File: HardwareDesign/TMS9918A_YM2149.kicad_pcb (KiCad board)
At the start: 2 copper layers, 150 x 90 mm, 46 parts, among them J001 Conn_02x40_Odd_Even, J701 RCJ-044, J702 Conn_01x02, J801 Conn_01x02, J802 Conn_02x09_Odd_Even, J803 SJ1-3525N, Q701 2N4401, U701 TMS9918A, U702 74HCT04, U703 74HCT32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

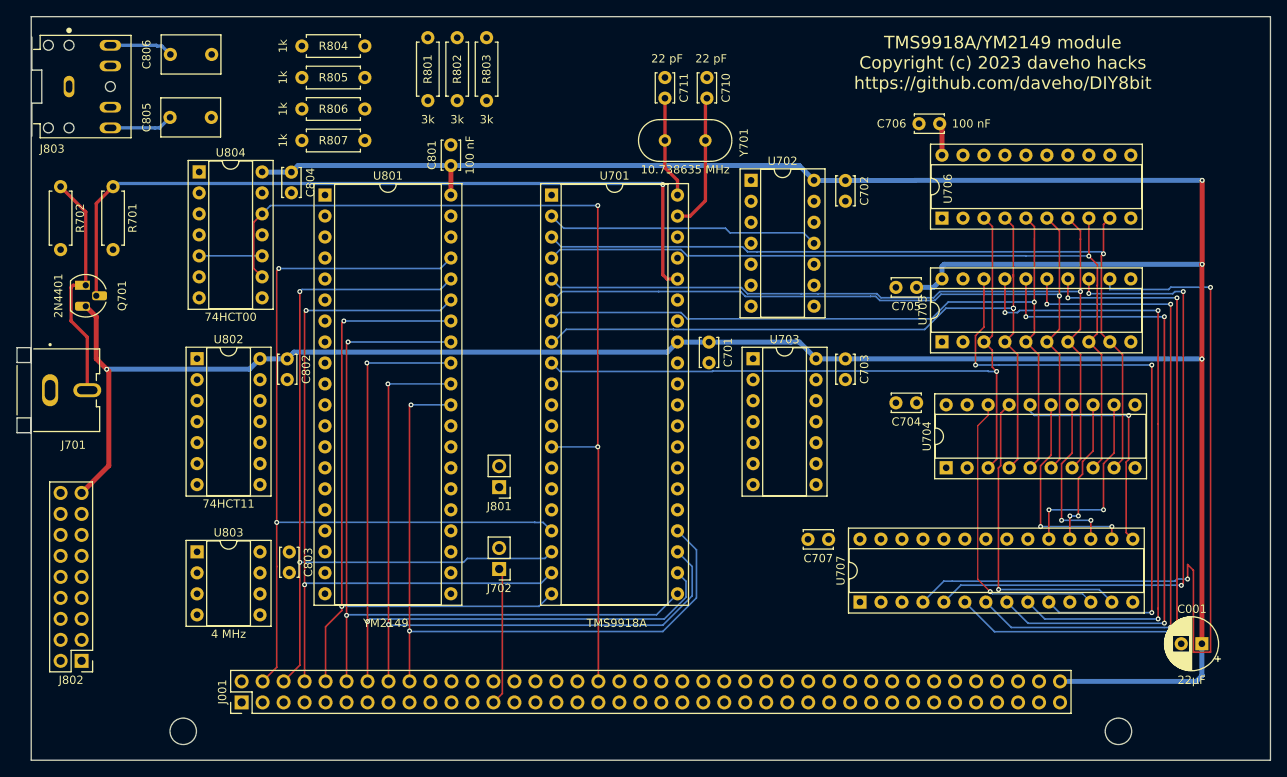
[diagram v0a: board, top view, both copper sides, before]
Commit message: completely started over on routing traces
Also, remove all Edge.Cuts lines from the 3.5mm audio jack
footprint. Not sure what those were supposed to be there
for, they definitely aren't needed.
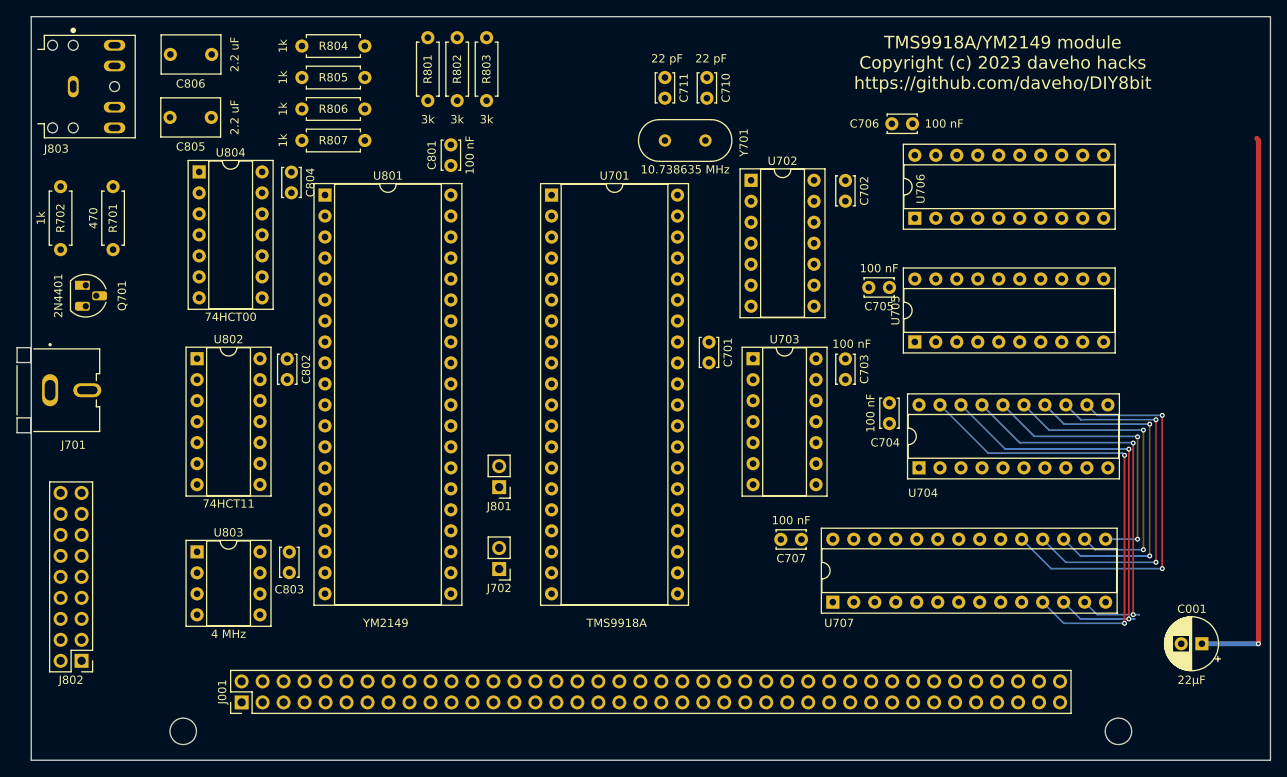
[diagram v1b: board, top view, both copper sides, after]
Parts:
- moved C704 3.29 mm to (167.4, 105.2), turned to -90 degrees
- moved C705 3.29 mm to (167.4, 91.2)
- moved C707 3.29 mm to (156.7, 121.7)
- moved U704 3.29 mm to (171.0, 113.0)
- moved U705 3.29 mm to (170.5, 97.8)
- moved U706 3.29 mm to (170.5, 82.8)
- moved U707 3.29 mm to (160.5, 129.3)
- moved C706 3.29 mm to (170.2, 71.4)
- moved J803 0.51 mm to (68.6, 66.9)
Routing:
- net VCC: track 396.4 -> 68.1 mm, vias 4 -> 1
- net /A0: track 113.0 -> 0.00 mm, vias 2 -> 0
- net /D0: track 105.8 -> 0.00 mm, vias 2 -> 0
- net /TMS9918ADisplay/VA6: track 105.7 -> 0.00 mm, vias 2 -> 0
- net /TMS9918ADisplay/AD7: track 99.8 -> 0.00 mm, vias 1 -> 0
- net /TMS9918ADisplay/AD6: track 98.2 -> 0.00 mm, vias 1 -> 0
- net /D1: track 97.9 -> 0.00 mm, vias 2 -> 0
- net /TMS9918ADisplay/AD5: track 97.8 -> 0.00 mm, vias 1 -> 0
- net /TMS9918ADisplay/AD4: track 95.3 -> 0.00 mm, vias 1 -> 0
- net /D4: track 94.7 -> 0.00 mm, vias 2 -> 0
- net Net-(Q701-Pad2): track 93.7 -> 0.00 mm, vias 1 -> 0
- net /D2: track 93.5 -> 0.00 mm, vias 2 -> 0
- net /TMS9918ADisplay/AD3: track 92.1 -> 0.00 mm, vias 1 -> 0
- net /D5: track 91.9 -> 0.00 mm, vias 2 -> 0
- net /TMS9918ADisplay/AD2: track 90.0 -> 0.00 mm, vias 2 -> 0
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
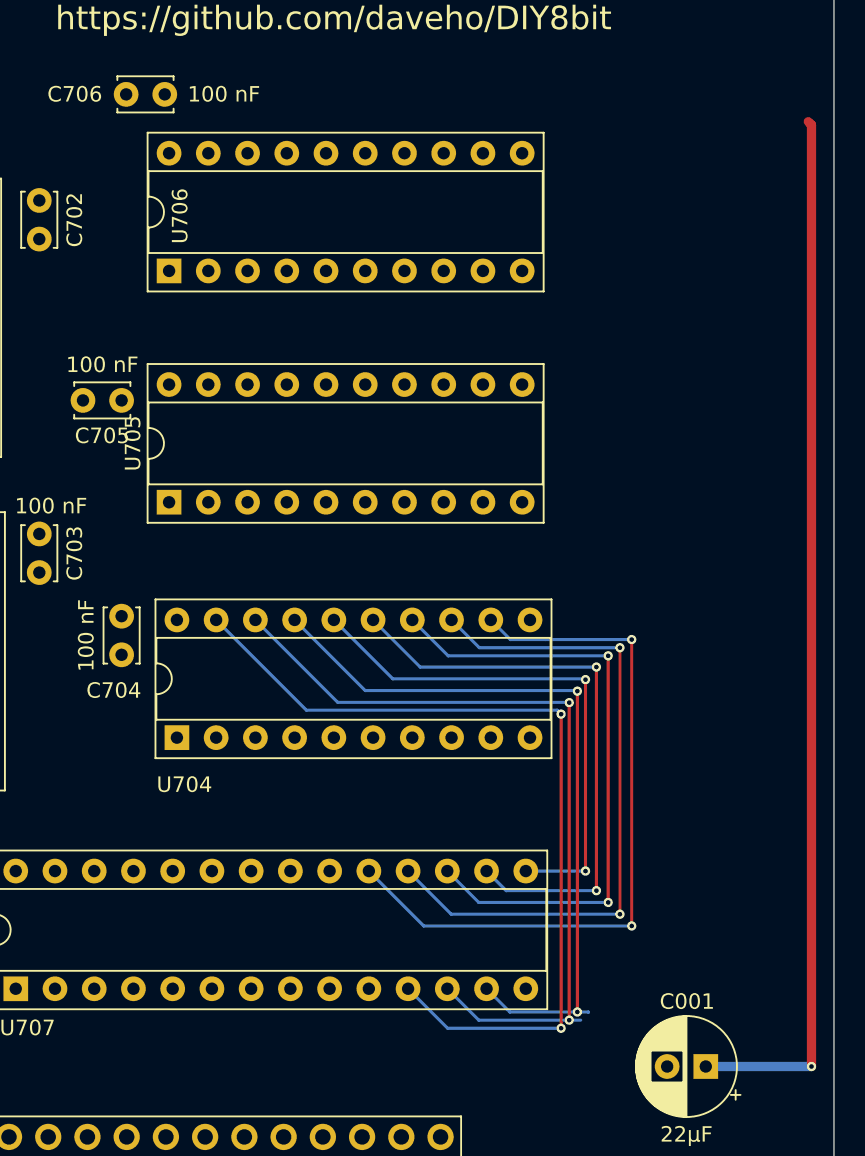
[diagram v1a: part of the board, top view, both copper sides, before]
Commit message: more routing of TMS9918A address/data reg signals
I think I have a viable strategy.
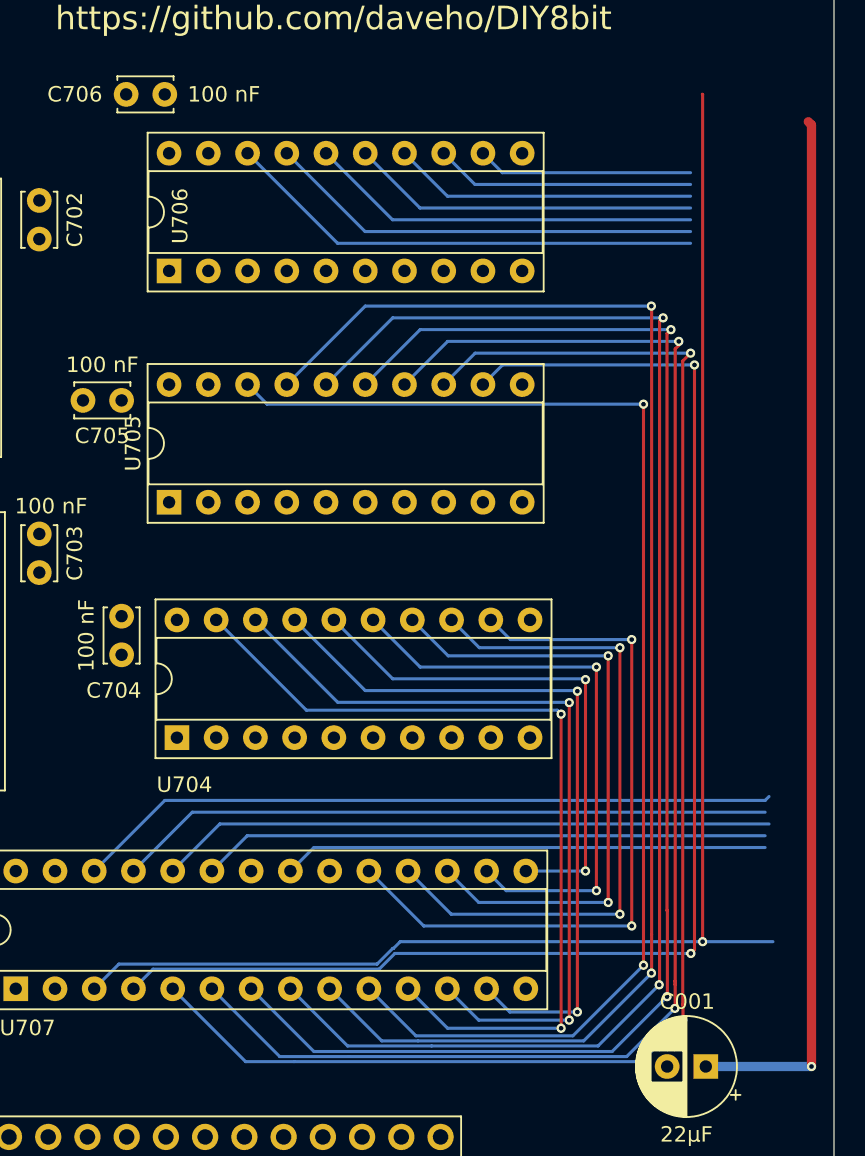
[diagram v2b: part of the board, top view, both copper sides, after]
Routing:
- net /TMS9918ADisplay/VA7: track 0.00 -> 131.2 mm, vias 0 -> 1
- net /TMS9918ADisplay/VA5: track 0.00 -> 96.3 mm, vias 0 -> 2
- net /TMS9918ADisplay/VA4: track 0.00 -> 95.5 mm, vias 0 -> 2
- net /TMS9918ADisplay/VA3: track 0.00 -> 94.6 mm, vias 0 -> 2
- net /TMS9918ADisplay/VA2: track 0.00 -> 94.2 mm, vias 0 -> 2
- net /TMS9918ADisplay/VA1: track 0.00 -> 93.0 mm, vias 0 -> 2
- net /TMS9918ADisplay/VA6: track 0.00 -> 89.4 mm, vias 0 -> 2
- net /TMS9918ADisplay/VA0: track 0.00 -> 83.4 mm, vias 0 -> 2
- net /TMS9918ADisplay/VA8: track 0.00 -> 70.7 mm
- net /TMS9918ADisplay/VA9: track 0.00 -> 65.3 mm
- net /TMS9918ADisplay/VA13: track 0.00 -> 59.7 mm
- net /TMS9918ADisplay/VA11: track 0.00 -> 56.4 mm
- net /TMS9918ADisplay/VA10: track 0.00 -> 53.9 mm
- net /TMS9918ADisplay/VA12: track 0.00 -> 16.8 mm
- net /TMS9918ADisplay/VD1: track 52.6 -> 51.8 mm
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
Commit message: routed more signals
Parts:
- moved J701 4.07 mm to (69.8, 103.9)
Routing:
- net VCC: track 68.1 -> 297.6 mm, vias 1 -> 5
- net /~{IODEV6}: track 0.00 -> 145.9 mm
- net /~{WMEM}: track 0.00 -> 145.2 mm, vias 0 -> 2
- net /~{RST}: track 0.00 -> 141.8 mm, vias 0 -> 3
- net /TMS9918ADisplay/VA12: track 16.8 -> 116.0 mm, vias 0 -> 2
- net /TMS9918ADisplay/V~{R}/W: track 0.00 -> 94.3 mm, vias 0 -> 3
- net /~{RMEM}: track 0.00 -> 63.9 mm, vias 0 -> 1
- net /TMS9918ADisplay/VR/~{W}: track 0.00 -> 63.6 mm, vias 0 -> 2
- net Net-(U702-Pad10): track 0.00 -> 51.6 mm, vias 0 -> 1
- net /TMS9918ADisplay/~{RAS}: track 0.00 -> 46.6 mm, vias 0 -> 1
- net /~{IODEV5}: track 0.00 -> 44.4 mm, vias 0 -> 1
- net /TMS9918ADisplay/VA13: track 59.7 -> 102.2 mm, vias 0 -> 2
- net /TMS9918ADisplay/VA11: track 56.4 -> 96.6 mm, vias 0 -> 2
- net /TMS9918ADisplay/VA10: track 53.9 -> 93.1 mm, vias 0 -> 2
- net /TMS9918ADisplay/VA9: track 65.3 -> 104.3 mm, vias 0 -> 2
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
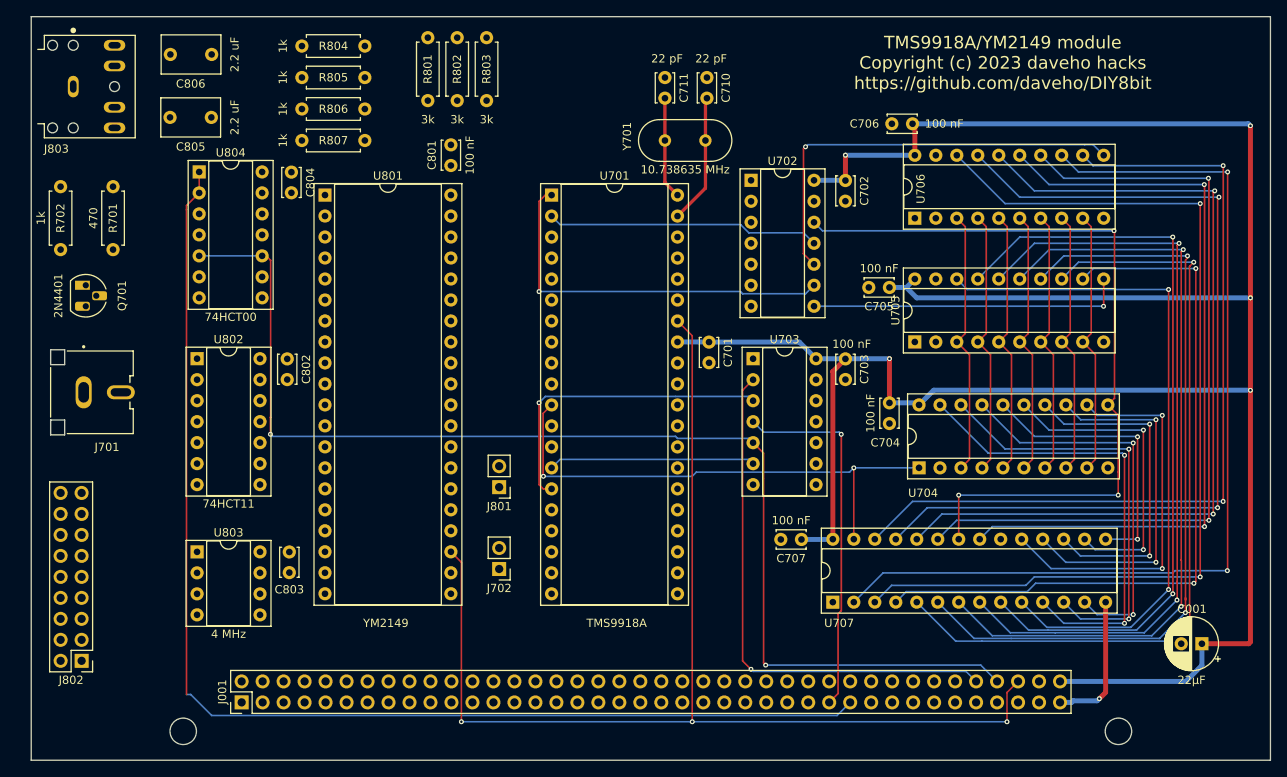
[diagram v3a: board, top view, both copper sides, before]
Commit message: TMS9918A section mostly done
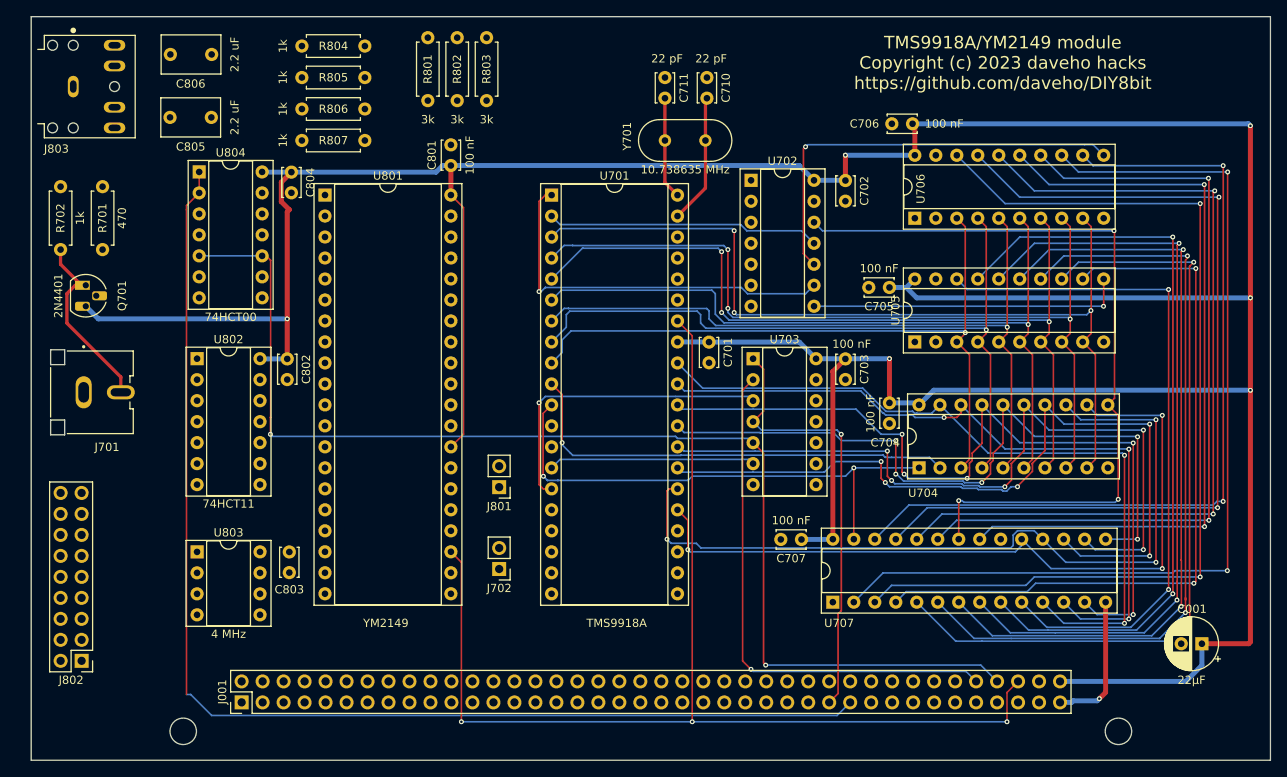
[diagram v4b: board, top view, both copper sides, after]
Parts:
- moved R701 7.73 mm to (72.1, 86.6), turned to 90 degrees
- moved R702 7.62 mm to (67.1, 86.6), turned to 90 degrees
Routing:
- net VCC: track 297.6 -> 452.7 mm, vias 5 -> 6
- net /TMS9918ADisplay/AD7: track 32.1 -> 108.2 mm, vias 0 -> 3
- net /TMS9918ADisplay/AD6: track 32.1 -> 103.8 mm, vias 0 -> 3
- net /TMS9918ADisplay/AD5: track 32.1 -> 102.2 mm, vias 0 -> 3
- net /TMS9918ADisplay/AD4: track 32.1 -> 93.6 mm, vias 0 -> 1
- net /TMS9918ADisplay/AD3: track 32.1 -> 89.7 mm, vias 0 -> 1
- net /TMS9918ADisplay/AD2: track 32.1 -> 88.7 mm, vias 0 -> 1
- net /TMS9918ADisplay/VD5: track 40.9 -> 97.0 mm, vias 2 -> 5
- net /TMS9918ADisplay/VD6: track 43.8 -> 98.9 mm, vias 2 -> 3
- net /TMS9918ADisplay/AD0: track 0.00 -> 54.8 mm, vias 0 -> 1
- net /TMS9918ADisplay/VD4: track 37.8 -> 92.2 mm, vias 2 -> 5
- net /TMS9918ADisplay/AD1: track 32.1 -> 84.9 mm, vias 0 -> 1
- net /TMS9918ADisplay/VD3: track 34.1 -> 86.7 mm, vias 2 -> 5
- net /TMS9918ADisplay/VD2: track 47.9 -> 98.9 mm, vias 2 -> 5
- net /TMS9918ADisplay/VD7: track 46.7 -> 93.6 mm, vias 2 -> 3
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
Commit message: routed more traces (getting there...)
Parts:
- moved J802 3.64 mm to (73.2, 137.2)
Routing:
- net /A0: track 0.00 -> 99.3 mm, vias 0 -> 2
- net /~{RMEM}: track 63.9 -> 161.5 mm, vias 1 -> 3
- net /D1: track 0.00 -> 90.0 mm, vias 0 -> 2
- net /D4: track 0.00 -> 87.9 mm, vias 0 -> 2
- net /D7: track 0.00 -> 86.4 mm, vias 0 -> 3
- net /D6: track 0.00 -> 85.3 mm, vias 0 -> 2
- net /D5: track 0.00 -> 85.2 mm, vias 0 -> 2
- net /D2: track 0.00 -> 83.8 mm, vias 0 -> 2
- net /D3: track 0.00 -> 77.2 mm, vias 0 -> 2
- net /D0: track 0.00 -> 48.3 mm, vias 0 -> 1
- net Net-(U802-Pad1): track 0.00 -> 19.1 mm, vias 0 -> 1
- net /~{IRQ2}: track 0.00 -> 16.8 mm
- net Net-(U802-Pad10): track 0.00 -> 14.1 mm, vias 0 -> 1
- net VCC: track 452.7 -> 452.2 mm
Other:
- board text added: "A0"
- board text added: "A7"
- board text added: "B0"
- board text added: "B7"
- board text added: "GND"
- board text added: "VCC"

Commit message: routed more signals
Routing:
- net Net-(Q701-Pad2): track 0.00 -> 77.3 mm
- net /YM2149_Sound/ANLG_A: track 0.00 -> 52.5 mm, vias 0 -> 1
- net VCC: track 452.2 -> 502.6 mm, vias 6 -> 7
- net /D0: track 48.3 -> 96.3 mm, vias 1 -> 2
- net /YM2149_Sound/ANLG_B: track 0.00 -> 38.6 mm, vias 0 -> 1
- net /YM2149_Sound/ANLG_C: track 0.00 -> 38.0 mm
- net /YM2149_Sound/TIP: track 0.00 -> 31.6 mm, vias 0 -> 1
- net /YM2149_Sound/BC1: track 0.00 -> 27.0 mm, vias 0 -> 1
- net /YM2149_Sound/RING: track 0.00 -> 26.2 mm, vias 0 -> 1
- net /YM2149_Sound/BDIR: track 0.00 -> 24.0 mm
- net Net-(U802-Pad1): track 19.1 -> 36.7 mm
- net Net-(U802-Pad11): track 0.00 -> 16.2 mm
- net Net-(U802-Pad10): track 14.1 -> 27.7 mm
- net Net-(C805-Pad2): track 0.00 -> 7.24 mm
- net Net-(C806-Pad2): track 0.00 -> 7.22 mm
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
